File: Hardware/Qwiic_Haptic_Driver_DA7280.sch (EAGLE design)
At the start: 21 parts, among them J1 QWIIC_RIGHT_ANGLE, J2 QWIIC_RIGHT_ANGLE

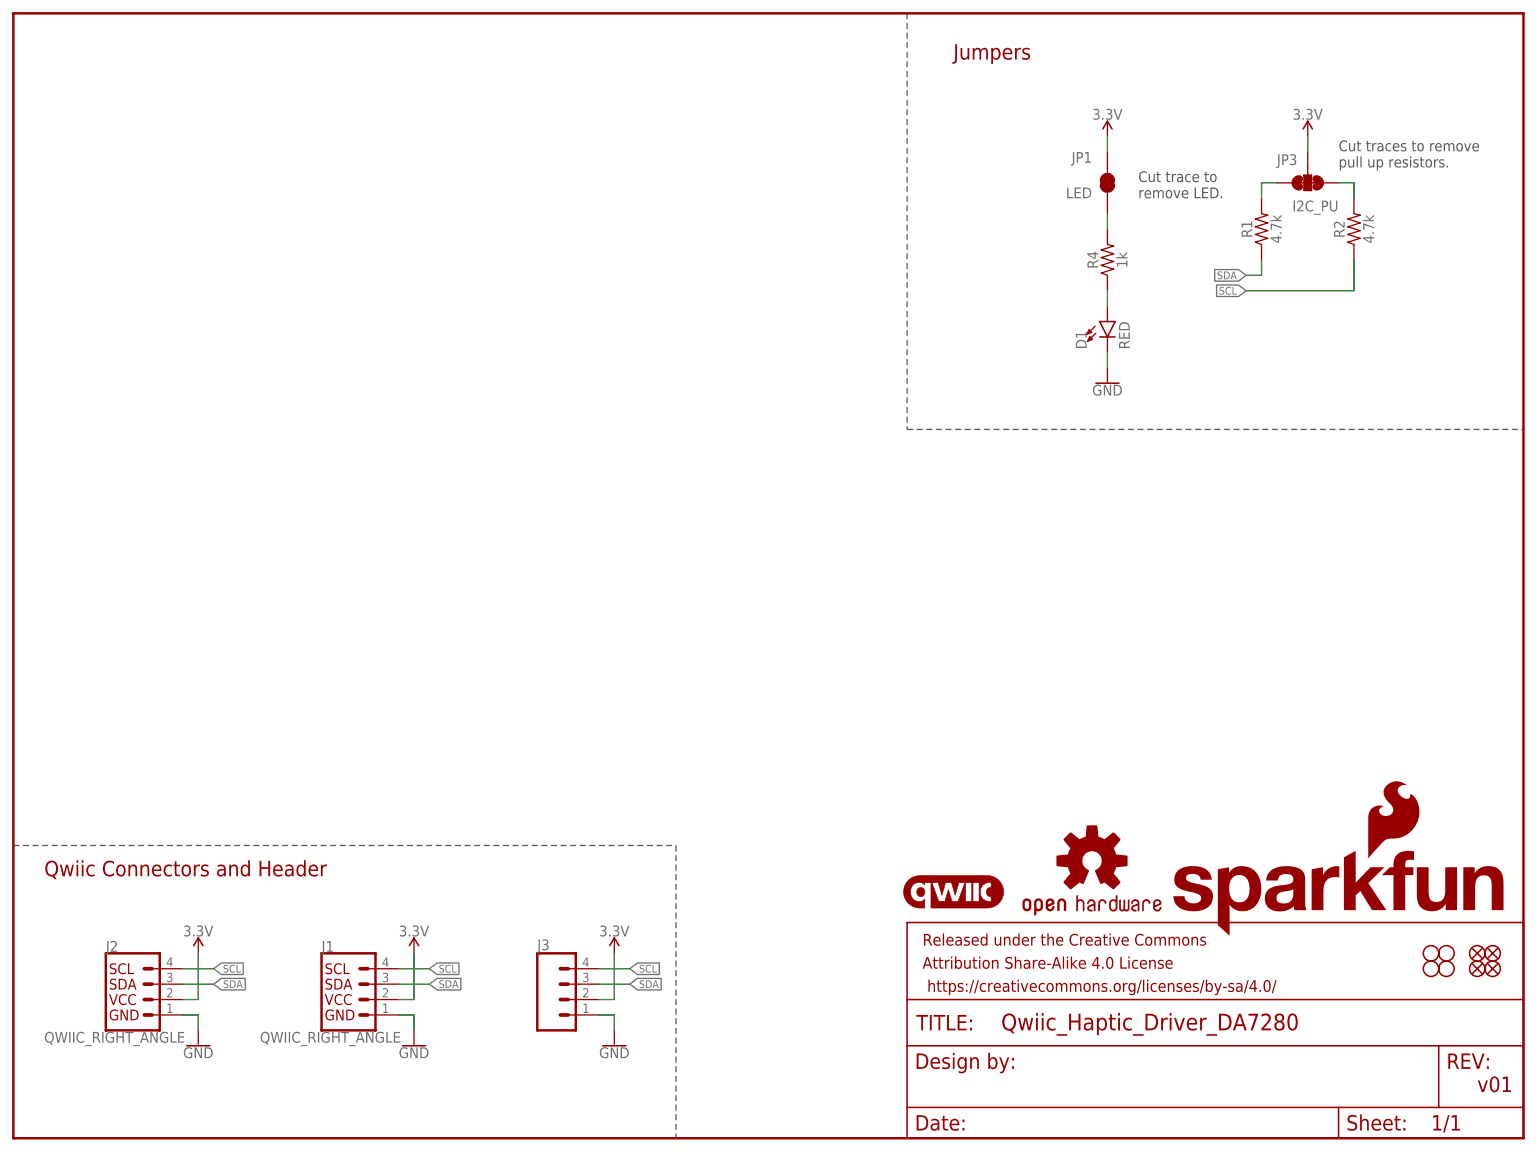
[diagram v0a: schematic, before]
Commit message: Fully routed the board - still needs silk
Minor changes to the DA7280:
* symbol size was shortened.
* Footprint was centered at 0,0
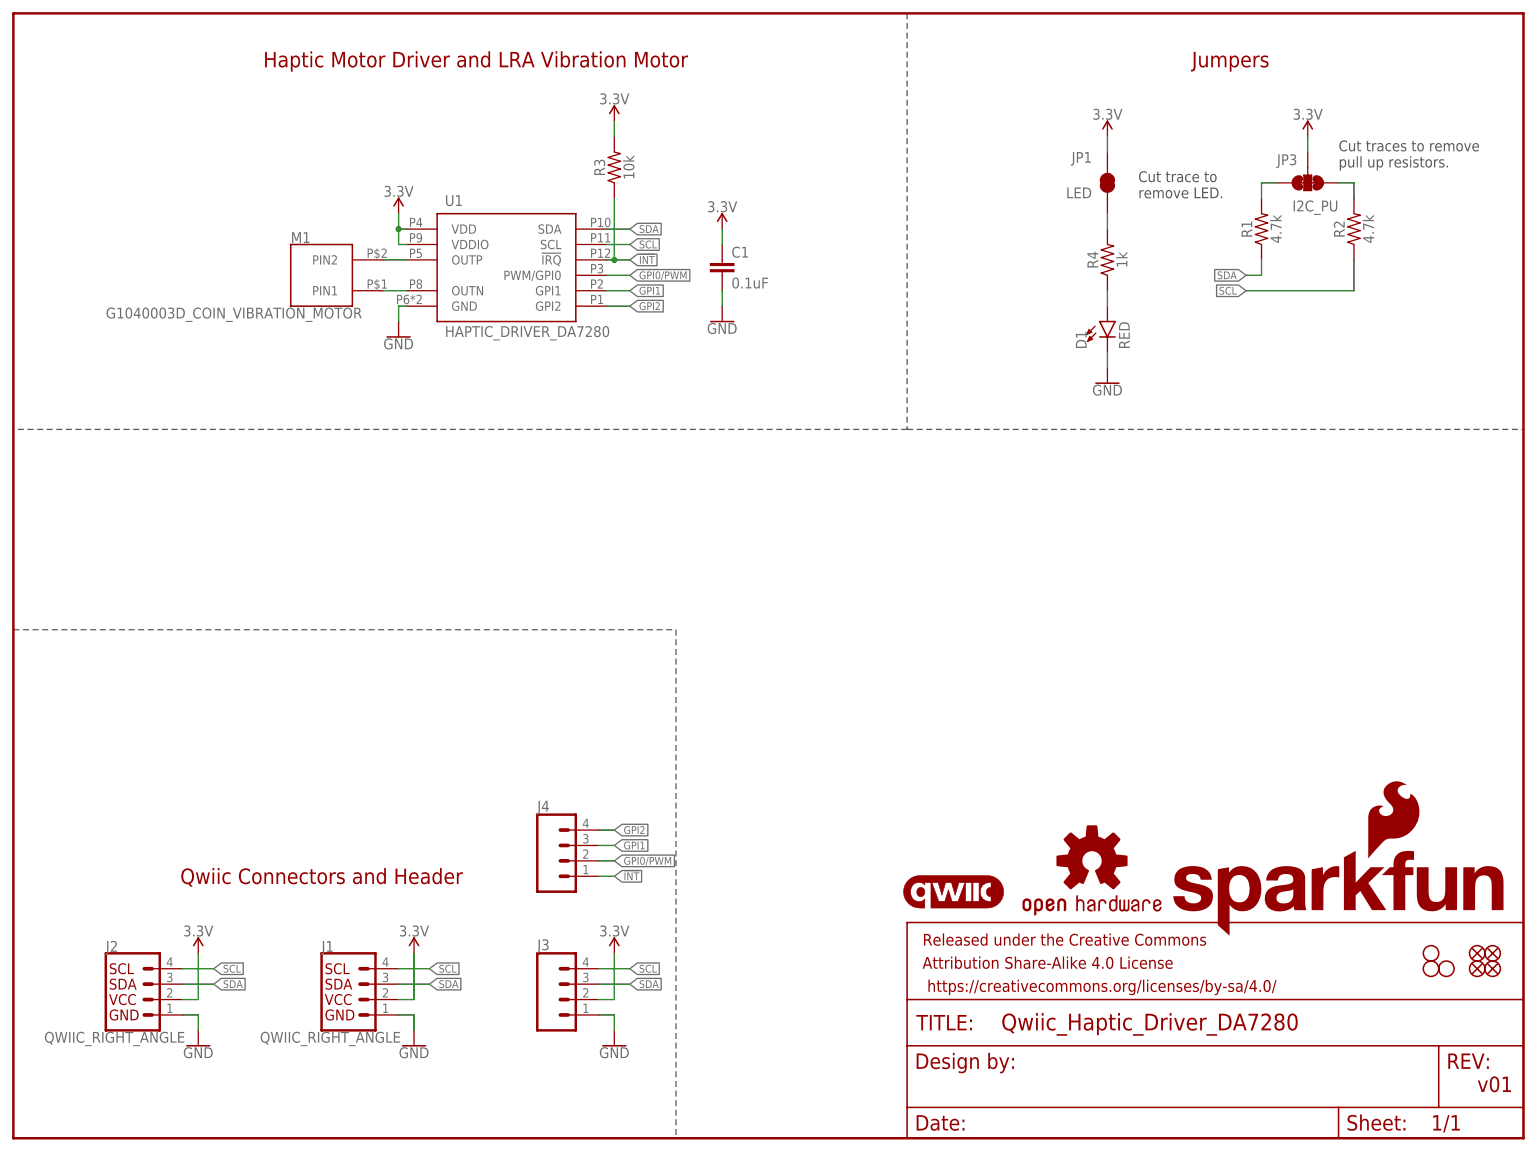
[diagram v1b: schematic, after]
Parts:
- removed H3: STAND-OFFTIGHT, SparkFun-Hardware:STAND-OFFTIGHT
- added C1: 0.1uF, SparkFun-Capacitors:0.1UF-0603-25V-5%
- added J4: (no value), SparkFun-Connectors:CONN_041X04_NO_SILK
- added M1: G1040003D_COIN_VIBRATION_MOTOR, TEMP:G1040003D_COIN_VIBRATION_MOTOR
- added R3: 10k, SparkFun-Resistors:10KOHM-0603-1/10W-1%
- added U1: HAPTIC_DRIVER_DA7280, TEMP:HAPTIC_DRIVER_DA7280
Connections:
- new net !INT!: J4.1, R3.1, U1.!IRQ!
- new net GPI0/PWM: J4.2, U1.PWM/GPI0
- new net GPI1: J4.3, U1.GPI1
- new net GPI2: J4.4, U1.GPI2
- new net N$5: M1.PIN2, U1.OUTP
- new net N$6: M1.PIN1, U1.OUTN
- net 3.3V: now also C1.1, R3.2, U1.VDD, U1.VDDIO
- net GND: now also C1.2, U1.GND
- net SCL: now also U1.SCL
- net SDA: now also U1.SDA
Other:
- note added: "Haptic Motor Driver and LRA Vibration Motor"

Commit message: Adds silk to PTH headers, cleans up schematic
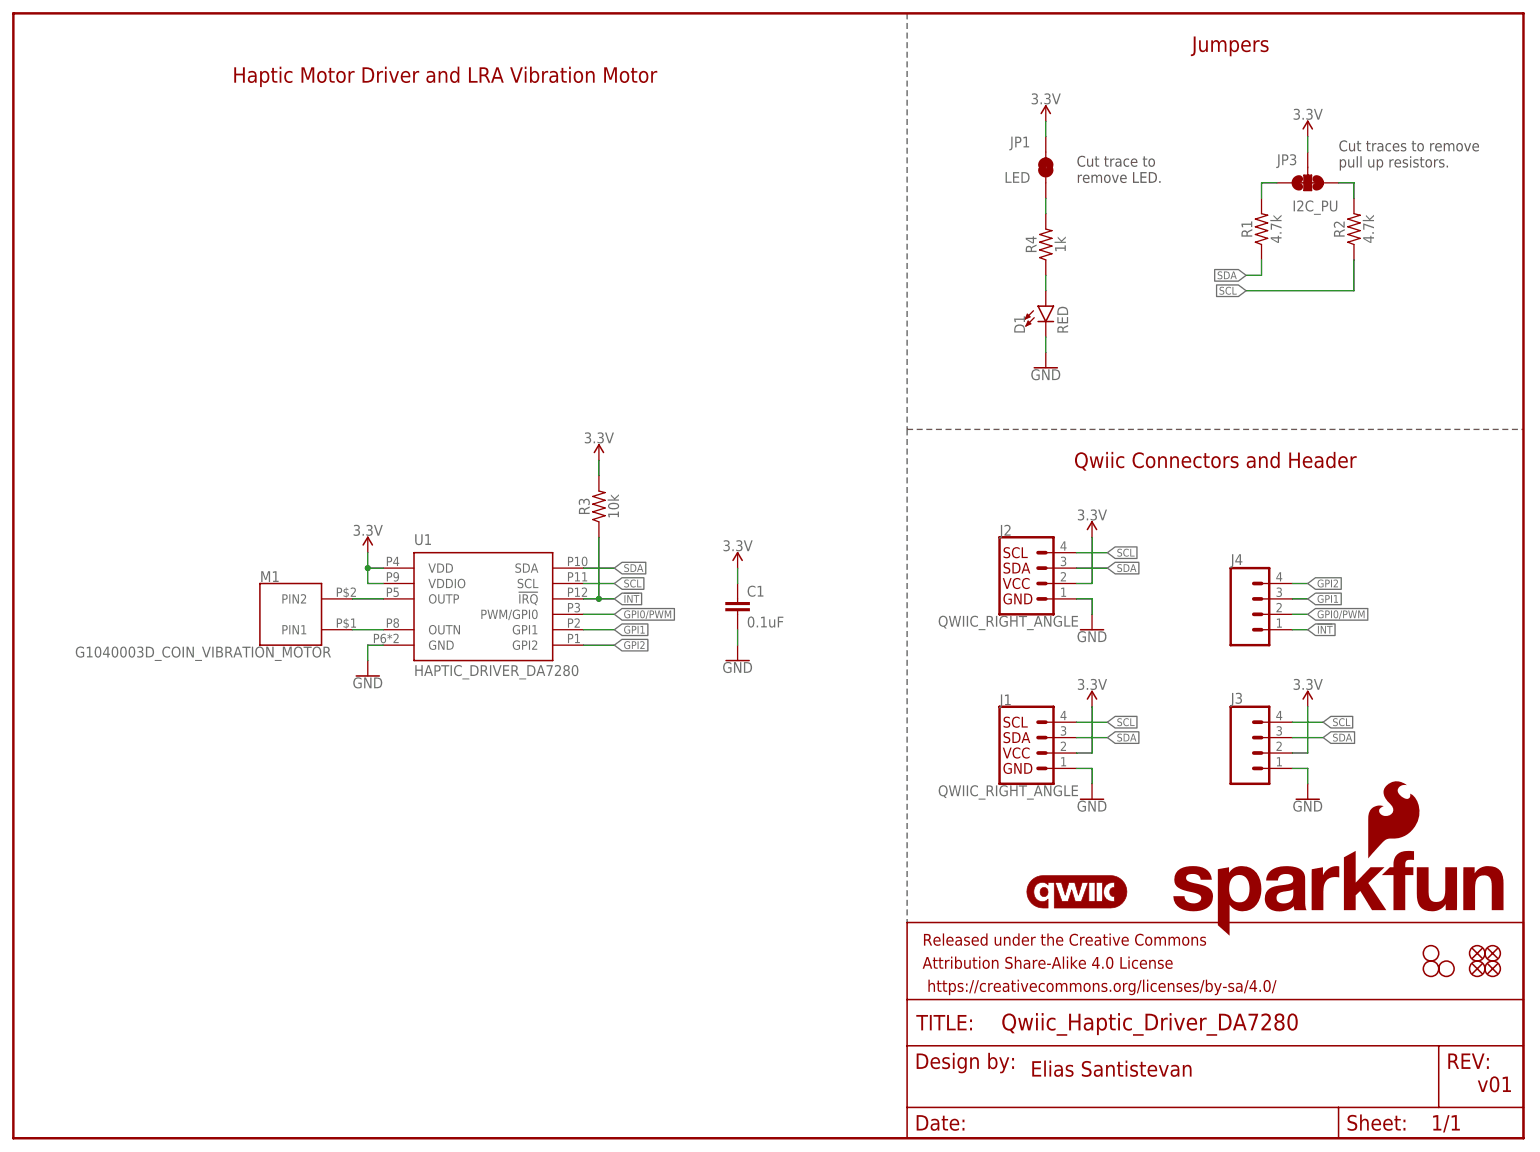
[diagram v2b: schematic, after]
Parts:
- removed LOGO2: OSHW-LOGOS, SparkFun-Aesthetics:OSHW-LOGOS
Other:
- note added: "Elias Santistevan"
- moved on the sheet: C1, D1, J1, J2, J3, J4, JP1, M1, R3, R4, U1

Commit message: Updates PTH headers to PTH headers with no PROD_ID
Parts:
- J3, J4: device SparkFun-Connectors:CONN_041X04_NO_SILK -> SparkFun-Connectors:CONN_041X04_NO_SILK_NO_POP
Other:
- moved on the sheet: J3
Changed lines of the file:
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@@
 <part name="J1" library="SparkFun-Connectors" deviceset="QWIIC_CONNECTOR" device="JS-1MM" value="QWIIC_RIGHT_ANGLE"/>
 <part name="J2" library="SparkFun-Connectors" deviceset="QWIIC_CONNECTOR" device="JS-1MM" value="QWIIC_RIGHT_ANGLE"/>
-<part name="J3" library="SparkFun-Connectors" deviceset="CONN_04" device="1X04_NO_SILK"/>
+<part name="J3" library="SparkFun-Connectors" deviceset="CONN_04" device="1X04_NO_SILK_NO_POP"/>
 <part name="R1" library="SparkFun-Resistors" deviceset="4.7KOHM" device="-0603-1/10W-1%" value="4.7k"/>
 <part name="R2" library="SparkFun-Resistors" deviceset="4.7KOHM" device="-0603-1/10W-1%" value="4.7k"/>
@@
 <part name="SUPPLY6" library="SparkFun-PowerSymbols" deviceset="3.3V" device=""/>
 <part name="GND6" library="SparkFun-PowerSymbols" deviceset="GND" device=""/>
-<part name="J4" library="SparkFun-Connectors" deviceset="CONN_04" device="1X04_NO_SILK"/>
+<part name="J4" library="SparkFun-Connectors" deviceset="CONN_04" device="1X04_NO_SILK_NO_POP"/>
 <part name="R3" library="SparkFun-Resistors" deviceset="10KOHM" device="-0603-1/10W-1%" value="10k"/>
 <part name="SUPPLY8" library="SparkFun-PowerSymbols" deviceset="3.3V" device=""/>
@@
 <attribute name="NAME" x="162.56" y="99.314" size="1.778" layer="95" font="vector"/>
 </instance>
-<instance part="J3" gate="J1" x="205.74" y="63.5" smashed="yes">
-<attribute name="VALUE" x="200.66" y="56.134" size="1.778" layer="96" font="vector"/>
-<attribute name="NAME" x="200.66" y="71.628" size="1.778" layer="95" font="vector"/>
+<instance part="J3" gate="J1" x="205.74" y="68.58" smashed="yes">
+<attribute name="VALUE" x="200.66" y="61.214" size="1.778" layer="96" font="vector"/>
+<attribute name="NAME" x="200.66" y="76.708" size="1.778" layer="95" font="vector"/>
 </instance>
 <instance part="R1" gate="G$1" x="205.74" y="149.86" smashed="yes" rot="R90">
@@
 <attribute name="VALUE" x="177.8" y="101.854" size="1.778" layer="96" font="vector" align="bottom-center"/>
 </instance>
-<instance part="SUPPLY4" gate="G$1" x="213.36" y="71.12" smashed="yes">
-<attribute name="VALUE" x="213.36" y="73.914" size="1.778" layer="96" font="vector" align="bottom-center"/>
+<instance part="SUPPLY4" gate="G$1" x="213.36" y="76.2" smashed="yes">
+<attribute name="VALUE" x="213.36" y="78.994" size="1.778" layer="96" font="vector" align="bottom-center"/>
 </instance>
 <instance part="GND2" gate="1" x="177.8" y="55.88" smashed="yes">
@@
 <attribute name="VALUE" x="177.8" y="83.566" size="1.778" layer="96" font="vector" align="top-center"/>
 </instance>
-<instance part="GND4" gate="1" x="213.36" y="55.88" smashed="yes">
-<attribute name="VALUE" x="213.36" y="55.626" size="1.778" layer="96" font="vector" align="top-center"/>
+<instance part="GND4" gate="1" x="213.36" y="60.96" smashed="yes">
+<attribute name="VALUE" x="213.36" y="60.706" size="1.778" layer="96" font="vector" align="top-center"/>
 </instance>
 <instance part="R4" gate="G$1" x="170.18" y="147.32" smashed="yes" rot="R90">
@@
 <segment>
 <pinref part="J3" gate="J1" pin="2"/>
-<wire x1="210.82" y1="63.5" x2="213.36" y2="63.5" width="0.1524" layer="91"/>
-<wire x1="213.36" y1="63.5" x2="213.36" y2="71.12" width="0.1524" layer="91"/>
+<wire x1="210.82" y1="68.58" x2="213.36" y2="68.58" width="0.1524" layer="91"/>
+<wire x1="213.36" y1="68.58" x2="213.36" y2="76.2" width="0.1524" layer="91"/>
 <pinref part="SUPPLY4" gate="G$1" pin="3.3V"/>
 </segment>
@@
 <pinref part="J3" gate="J1" pin="1"/>
 <pinref part="GND4" gate="1" pin="GND"/>
-<wire x1="210.82" y1="60.96" x2="213.36" y2="60.96" width="0.1524" layer="91"/>
-<wire x1="213.36" y1="60.96" x2="213.36" y2="58.42" width="0.1524" layer="91"/>
+<wire x1="210.82" y1="66.04" x2="213.36" y2="66.04" width="0.1524" layer="91"/>
+<wire x1="213.36" y1="66.04" x2="213.36" y2="63.5" width="0.1524" layer="91"/>
 </segment>
 <segment>
@@
 <segment>
 <pinref part="J3" gate="J1" pin="4"/>
-<wire x1="210.82" y1="68.58" x2="215.9" y2="68.58" width="0.1524" layer="91"/>
-<label x="215.9" y="68.58" size="1.27" layer="95" font="vector" xref="yes"/>
+<wire x1="210.82" y1="73.66" x2="215.9" y2="73.66" width="0.1524" layer="91"/>
+<label x="215.9" y="73.66" size="1.27" layer="95" font="vector" xref="yes"/>
 </segment>
 <segment>
@@
 <segment>
 <pinref part="J3" gate="J1" pin="3"/>
-<wire x1="210.82" y1="66.04" x2="215.9" y2="66.04" width="0.1524" layer="91"/>
-<label x="215.9" y="66.04" size="1.27" layer="95" font="vector" xref="yes"/>
-</segment>
-<segment>
+<wire x1="210.82" y1="71.12" x2="215.9" y2="71.12" width="0.1524" layer="91"/>
+<label x="215.9" y="71.12" size="1.27" layer="95" font="vector" xref="yes"/>
+</segment>
+<segment>

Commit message: Moves PTH interrupt closer to GND PTH hold and shifts all the GPI down.
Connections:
- net !INT!: now also J4.4; no longer J4.1
- net GPI0/PWM: now also J4.1; no longer J4.2
- net GPI1: now also J4.2; no longer J4.3
- net GPI2: now also J4.3; no longer J4.4
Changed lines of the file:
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@@
 </segment>
 <segment>
-<pinref part="J4" gate="J1" pin="1"/>
-<wire x1="210.82" y1="83.82" x2="213.36" y2="83.82" width="0.1524" layer="91"/>
-<label x="213.36" y="83.82" size="1.27" layer="95" font="vector" xref="yes"/>
+<wire x1="210.82" y1="91.44" x2="213.36" y2="91.44" width="0.1524" layer="91"/>
+<label x="213.36" y="91.44" size="1.27" layer="95" font="vector" xref="yes"/>
+<pinref part="J4" gate="J1" pin="4"/>
 </segment>
 </net>
@@
 </segment>
 <segment>
-<pinref part="J4" gate="J1" pin="3"/>
-<wire x1="210.82" y1="88.9" x2="213.36" y2="88.9" width="0.1524" layer="91"/>
-<label x="213.36" y="88.9" size="1.27" layer="95" font="vector" xref="yes"/>
+<wire x1="210.82" y1="86.36" x2="213.36" y2="86.36" width="0.1524" layer="91"/>
+<label x="213.36" y="86.36" size="1.27" layer="95" font="vector" xref="yes"/>
+<pinref part="J4" gate="J1" pin="2"/>
 </segment>
 </net>
@@
 </segment>
 <segment>
-<pinref part="J4" gate="J1" pin="4"/>
-<wire x1="210.82" y1="91.44" x2="213.36" y2="91.44" width="0.1524" layer="91"/>
-<label x="213.36" y="91.44" size="1.27" layer="95" font="vector" xref="yes"/>
+<wire x1="210.82" y1="88.9" x2="213.36" y2="88.9" width="0.1524" layer="91"/>
+<label x="213.36" y="88.9" size="1.27" layer="95" font="vector" xref="yes"/>
+<pinref part="J4" gate="J1" pin="3"/>
 </segment>
 </net>
@@
 <net name="GPI0/PWM" class="0">
 <segment>
-<pinref part="J4" gate="J1" pin="2"/>
-<wire x1="210.82" y1="86.36" x2="213.36" y2="86.36" width="0.1524" layer="91"/>
-<label x="213.36" y="86.36" size="1.27" layer="95" font="vector" xref="yes"/>
-</segment>
-<segment>
 <pinref part="U1" gate="G$1" pin="PWM/GPI0"/>
 <wire x1="99.06" y1="86.36" x2="93.98" y2="86.36" width="0.1524" layer="91"/>
 <label x="99.06" y="86.36" size="1.27" layer="95" font="vector" xref="yes"/>
 </segment>
+<segment>
+<wire x1="210.82" y1="83.82" x2="213.36" y2="83.82" width="0.1524" layer="91"/>
+<label x="213.36" y="83.82" size="1.27" layer="95" font="vector" xref="yes"/>
+<pinref part="J4" gate="J1" pin="1"/>
+</segment>
 </net>

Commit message: Adds new package for the vibration motor - one that will go through the PCB
* The new package has castellated leads to the part was rotated 180 degrees to the edge of the board.
* Fixes interrupt silk to reflect active low
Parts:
- removed LOGO1: SFE_LOGO_NAME_FLAME.1_INCH, SparkFun-Aesthetics:SFE_LOGO_NAME_FLAME.1_INCH
- M1: value G1040003D_COIN_VIBRATION_MOTOR -> G1040003D_LRA_CASTELLATED; device TEMP:G1040003D_COIN_VIBRATION_MOTOR -> TEMP:G1040003D_LRA_CASTELLATED
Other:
- moved on the sheet: M1
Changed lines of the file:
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@@
 <part name="R1" library="SparkFun-Resistors" deviceset="4.7KOHM" device="-0603-1/10W-1%" value="4.7k"/>
 <part name="R2" library="SparkFun-Resistors" deviceset="4.7KOHM" device="-0603-1/10W-1%" value="4.7k"/>
-<part name="LOGO1" library="SparkFun-Aesthetics" deviceset="SFE_LOGO_NAME_FLAME" device=".1_INCH" value="SFE_LOGO_NAME_FLAME.1_INCH"/>
 <part name="U$1" library="SparkFun-Aesthetics" deviceset="QWIIC_LOGO" device="_5MM"/>
 <part name="SUPPLY2" library="SparkFun-PowerSymbols" deviceset="3.3V" device=""/>
@@
 <part name="SUPPLY7" library="SparkFun-PowerSymbols" deviceset="3.3V" device=""/>
 <part name="U1" library="TEMP" deviceset="HAPTIC_DRIVER_DA7280" device=""/>
-<part name="M1" library="TEMP" deviceset="G1040003D_COIN_VIBRATION_MOTOR" device=""/>
+<part name="M1" library="TEMP" deviceset="G1040003D_LRA" device="_CASTELLATED" value="G1040003D_LRA_CASTELLATED"/>
 <part name="SUPPLY1" library="SparkFun-PowerSymbols" deviceset="3.3V" device=""/>
 <part name="GND1" library="SparkFun-PowerSymbols" deviceset="GND" device=""/>
@@
 <attribute name="VALUE" x="222.504" y="149.86" size="1.778" layer="96" font="vector" rot="R90" align="top-center"/>
 </instance>
-<instance part="LOGO1" gate="G$1" x="190.5" y="33.02" smashed="yes"/>
 <instance part="U$1" gate="G$1" x="175.26" y="40.64" smashed="yes"/>
 <instance part="SUPPLY2" gate="G$1" x="177.8" y="71.12" smashed="yes">
@@
 <attribute name="VALUE" x="66.04" y="76.2" size="1.778" layer="96"/>
 </instance>
-<instance part="M1" gate="G$1" x="45.72" y="86.36" smashed="yes" rot="MR180">
-<attribute name="NAME" x="40.64" y="93.472" size="1.778" layer="95" rot="MR180"/>
-<attribute name="VALUE" x="10.16" y="81.026" size="1.778" layer="95" rot="MR180"/>
+<instance part="M1" gate="G$1" x="40.64" y="86.36" smashed="yes" rot="MR180">
+<attribute name="NAME" x="35.56" y="93.472" size="1.778" layer="95" rot="MR180"/>
+<attribute name="VALUE" x="18.288" y="80.264" size="1.778" layer="95" rot="MR180"/>
 </instance>
 <instance part="SUPPLY1" gate="G$1" x="58.42" y="96.52" smashed="yes">
@@
 </segment>
 </net>
-<net name="N$5" class="0">
-<segment>
-<pinref part="U1" gate="G$1" pin="OUTP"/>
-<pinref part="M1" gate="G$1" pin="PIN2"/>
-<wire x1="60.96" y1="88.9" x2="55.88" y2="88.9" width="0.1524" layer="91"/>
-</segment>
-</net>
-<net name="N$6" class="0">
-<segment>
-<pinref part="U1" gate="G$1" pin="OUTN"/>
-<pinref part="M1" gate="G$1" pin="PIN1"/>
-<wire x1="60.96" y1="83.82" x2="55.88" y2="83.82" width="0.1524" layer="91"/>
-</segment>
-</net>
 <net name="GPI0/PWM" class="0">
 <segment>
@@
 </segment>
 </net>
+<net name="N$5" class="0">
+<segment>
+<pinref part="U1" gate="G$1" pin="OUTN"/>
+<pinref part="M1" gate="G$1" pin="PIN1"/>
+<wire x1="60.96" y1="83.82" x2="50.8" y2="83.82" width="0.1524" layer="91"/>
+</segment>
+</net>
+<net name="N$6" class="0">
+<segment>
+<pinref part="U1" gate="G$1" pin="OUTP"/>
+<pinref part="M1" gate="G$1" pin="PIN2"/>
+<wire x1="60.96" y1="88.9" x2="50.8" y2="88.9" width="0.1524" layer="91"/>
+</segment>
+</net>
